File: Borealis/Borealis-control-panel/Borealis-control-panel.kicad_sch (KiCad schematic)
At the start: 0 parts

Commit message: Update control panel schematic
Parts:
- added Brd1: SSD1306, TG9541:Display_128x64_096_I2C, symbol SSD1306-128x64_OLED:SSD1306
- added D1, D2: LED, LED_THT:LED_D5.0mm, symbol Device:LED
- added J2: Conn_01x08_Pin, Connector_JST:JST_PH_B8B-PH-K_1x08_P2.00mm_Vertical, symbol Connector:Conn_01x08_Pin
- added SW1, SW2: SW_SPDT, Connector_PinHeader_2.54mm:PinHeader_1x03_P2.54mm_Vertical, symbol Switch:SW_SPDT
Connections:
- new net: Brd1.1 (GND), D1.1 (K), D2.1 (K), J2.1 (Pin_1), SW2.1 (A)
- new net: Brd1.2 (VCC), J2.2 (Pin_2), SW1.2 (B), SW1.3 (C)
- new net: Brd1.3 (SCL), J2.3 (Pin_3)
- new net: Brd1.4 (SDA), J2.4 (Pin_4)
- new net: D2.2 (A), J2.5 (Pin_5)
- new net: D1.2 (A), J2.6 (Pin_6)
- new net: J2.7 (Pin_7), SW1.1 (A)
- new net: J2.8 (Pin_8), SW2.2 (B), SW2.3 (C)

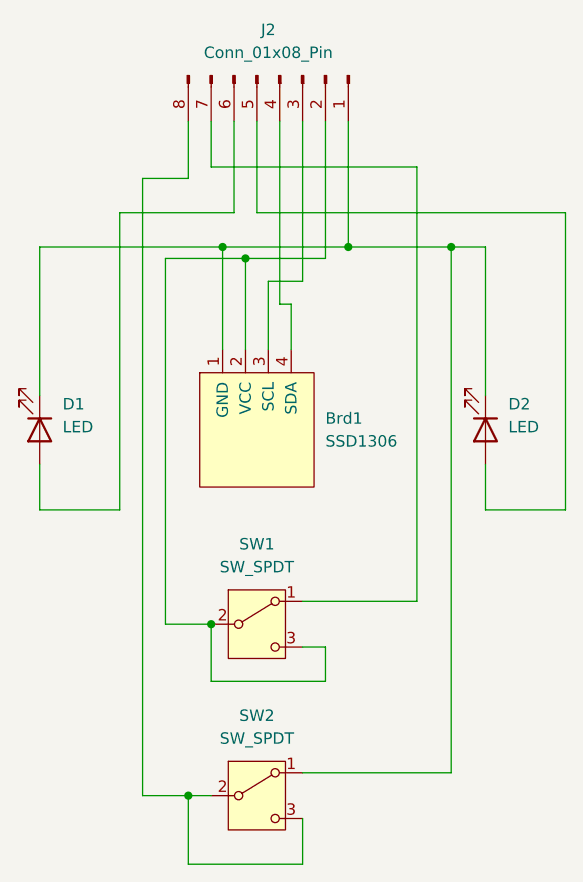
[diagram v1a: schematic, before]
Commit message: Added sensor board
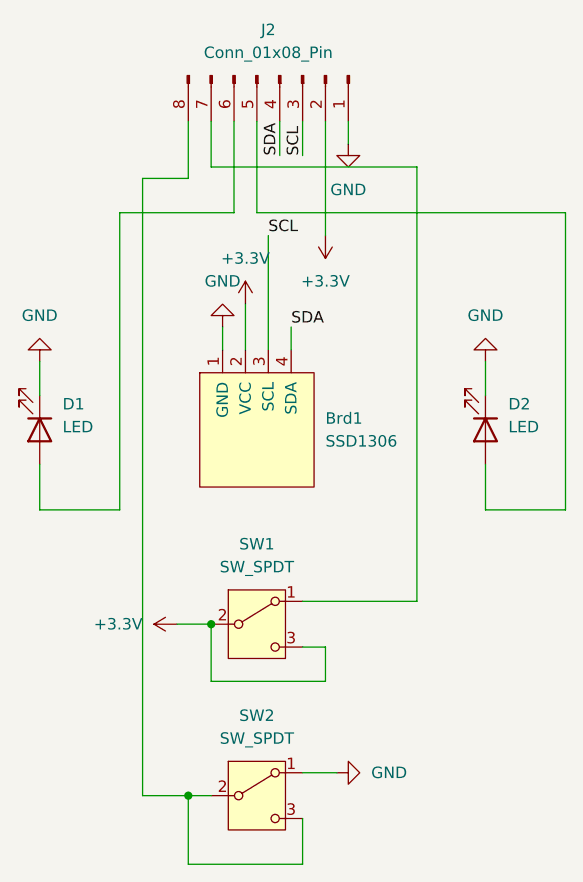
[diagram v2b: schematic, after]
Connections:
- net GND: now reaches Brd1.1 (GND), D1.1 (K), D2.1 (K), J2.1 (Pin_1), SW2.1 (A)
- net +3.3V: now reaches Brd1.2 (VCC), J2.2 (Pin_2), SW1.2 (B), SW1.3 (C)
- net SCL: now reaches Brd1.3 (SCL), J2.3 (Pin_3)
- net SDA: now reaches Brd1.4 (SDA), J2.4 (Pin_4)
